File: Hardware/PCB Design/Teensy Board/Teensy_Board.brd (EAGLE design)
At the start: 98.7 x 81.3 mm, 40 parts, among them IC1 MC7805BDTRKG, IC2 UA78M33CKVU, Q1 PROGRAM_FET, U1 PCA9685PW, U2 74HC4051PW,118, U3 74HC4051PW,118, X1 RJ45-8X, X2 RJ45-8X, X3 RJ45-8X, X4 RJ45-8X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

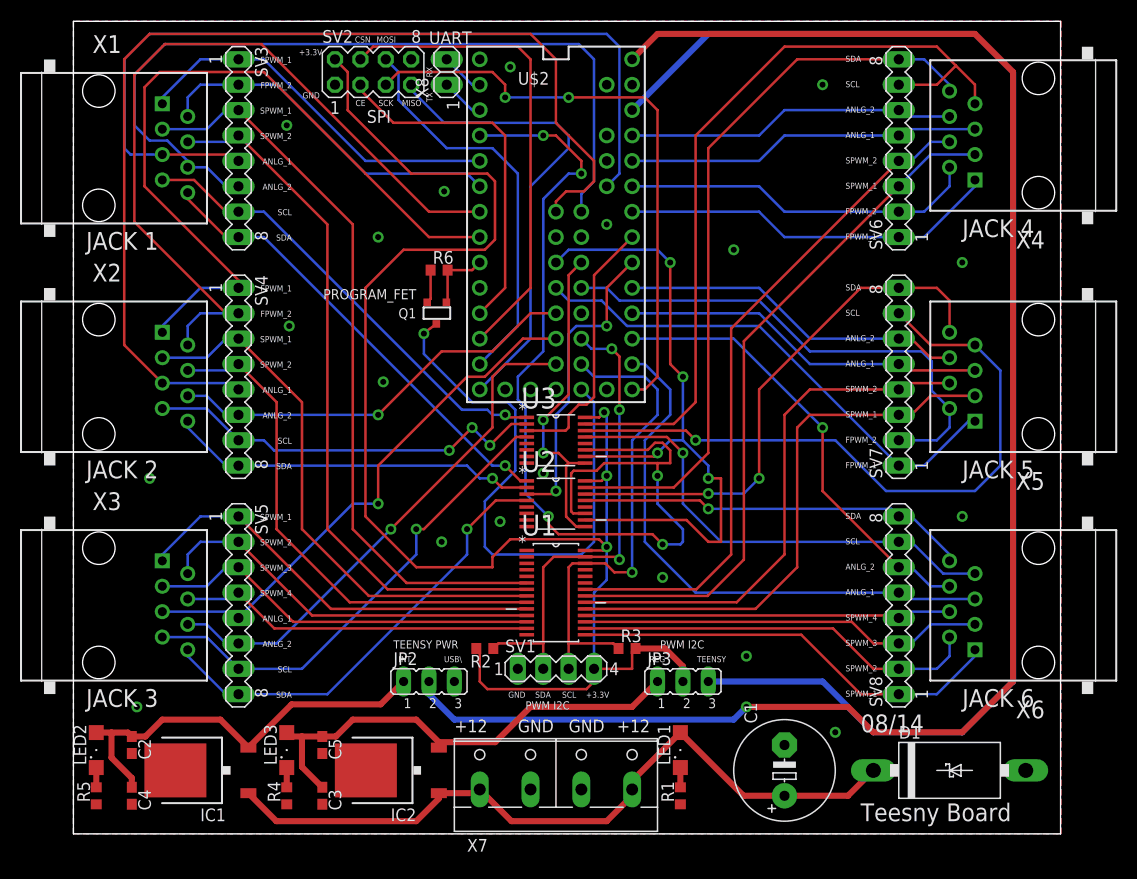
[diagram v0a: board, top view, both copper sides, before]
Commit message: Added 4 more power ports; added pull up resistor; made a power plate for the power
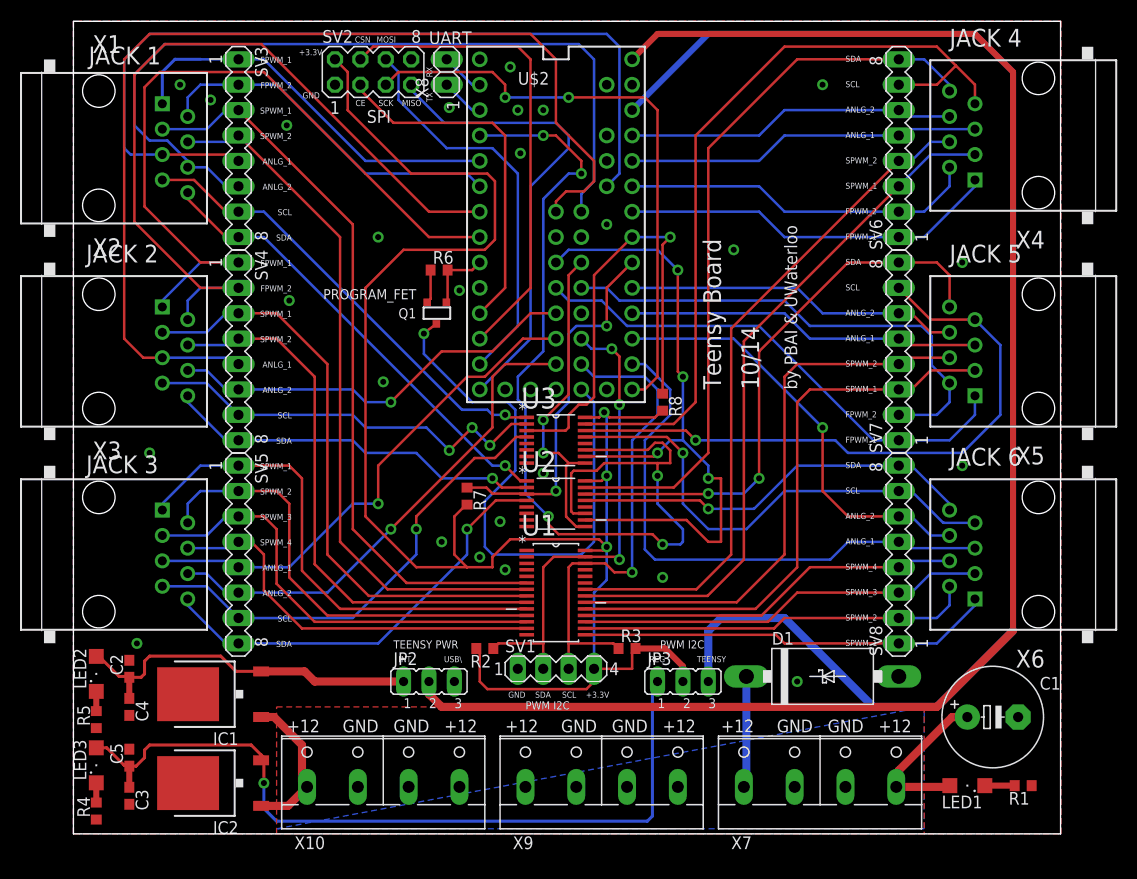
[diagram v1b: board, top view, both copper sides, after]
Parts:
- added R7, R8: (no value), CBLA_Test_bed_Library:R0603
- added X10, X9: (no value), con-wago-508:W237-4P
- moved R1 34.3 mm to (95.0, 4.83), turned to 180 degrees
- moved LED1 28.9 mm to (89.4, 4.83), turned to 180 degrees
- moved X7 26.4 mm to (74.7, 5.33)
- moved C1 21.5 mm to (91.9, 11.7), turned to 0 degrees
- moved C5 19.3 mm to (5.59, 7.62), turned to 90 degrees
- moved C3 19.3 mm to (5.59, 3.81)
- moved LED3 19.1 mm to (2.29, 6.86)
- moved R4 19.1 mm to (2.29, 2.29)
- moved IC2 17.8 mm to (14.0, 5.08)
- moved D1 15.8 mm to (74.9, 15.7)
- moved C4 8.89 mm to (5.59, 12.7)
- moved IC1 7.73 mm to (14.0, 14.0)
- moved C2 7.62 mm to (5.59, 16.5), turned to 90 degrees
- moved LED2 7.62 mm to (2.29, 16.0)
- moved R5 7.62 mm to (2.29, 11.4)
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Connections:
- net +12V: now also X10.1, X10.4, X9.1, X9.4
- net 3V3INT: now also R7.2, R8.2
- net GND: now also X10.2, X10.3, X9.2, X9.3
- net MUL_SCL: now also R8.1
- net MUL_SDA: now also R7.1
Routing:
- net +3V3: track 47.9 -> 80.4 mm, vias 0 -> 1
- net +12V: track 74.8 -> 42.4 mm
- net MUL_SCL: track 26.4 -> 46.2 mm, vias 0 -> 1
- net 3V3INT: track 158.1 -> 171.8 mm
- net SPWM_3_1: track 42.5 -> 50.0 mm
- net SPWM_3_2: track 39.4 -> 45.8 mm
- net MUL_SDA: track 30.8 -> 37.1 mm
- net TEENSY_VIN: track 166.1 -> 160.0 mm, vias 1 -> 0
- net +5V: track 41.8 -> 36.4 mm
- net SPWM_3_3: track 39.5 -> 44.8 mm
- net SPWM_2_1: track 55.3 -> 60.1 mm
- net SPWM_2_2: track 51.5 -> 56.1 mm
- net SPWM_3_4: track 35.7 -> 39.9 mm
- net MUL_SCL_5: track 67.1 -> 63.5 mm
- net SPWM_5_2: track 53.7 -> 57.0 mm
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- added copper zone on layer 1, net +12V
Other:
- board text added: "10/14"
- board text added: "Teensy Board"
- board text added: "by PBAI & UWaterloo"
- board text removed: "08/14"
- board text removed: "Teesny Board"
